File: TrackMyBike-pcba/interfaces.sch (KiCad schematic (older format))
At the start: 1 part

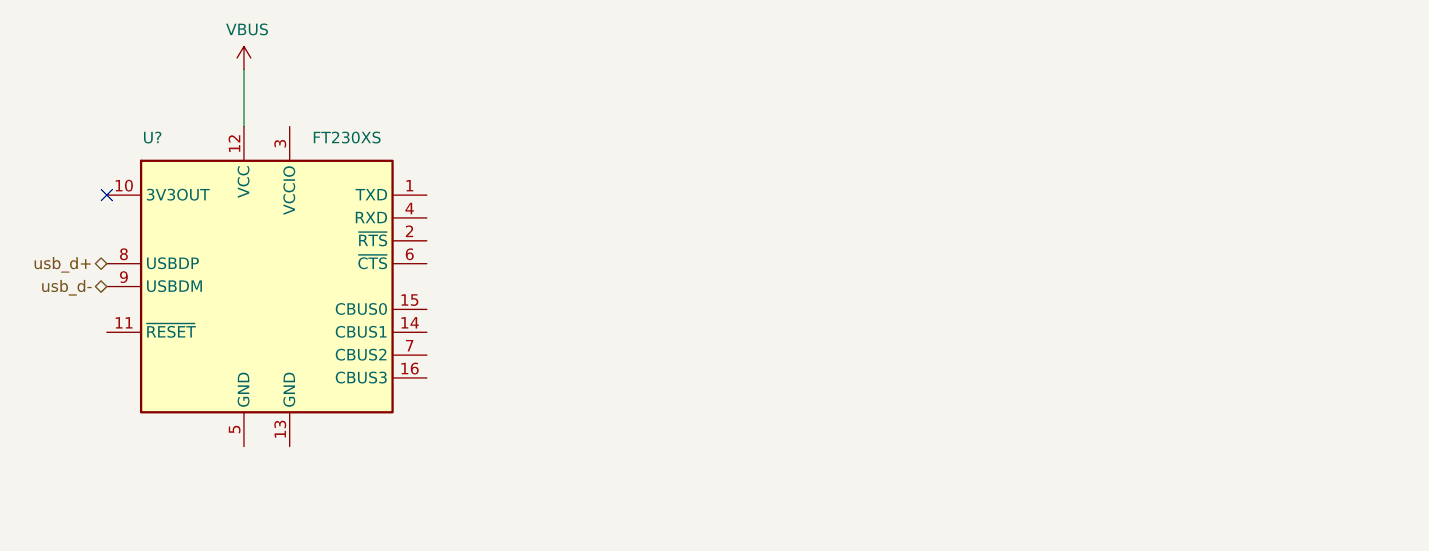
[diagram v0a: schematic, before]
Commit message: Add SIM card, FTDI IC
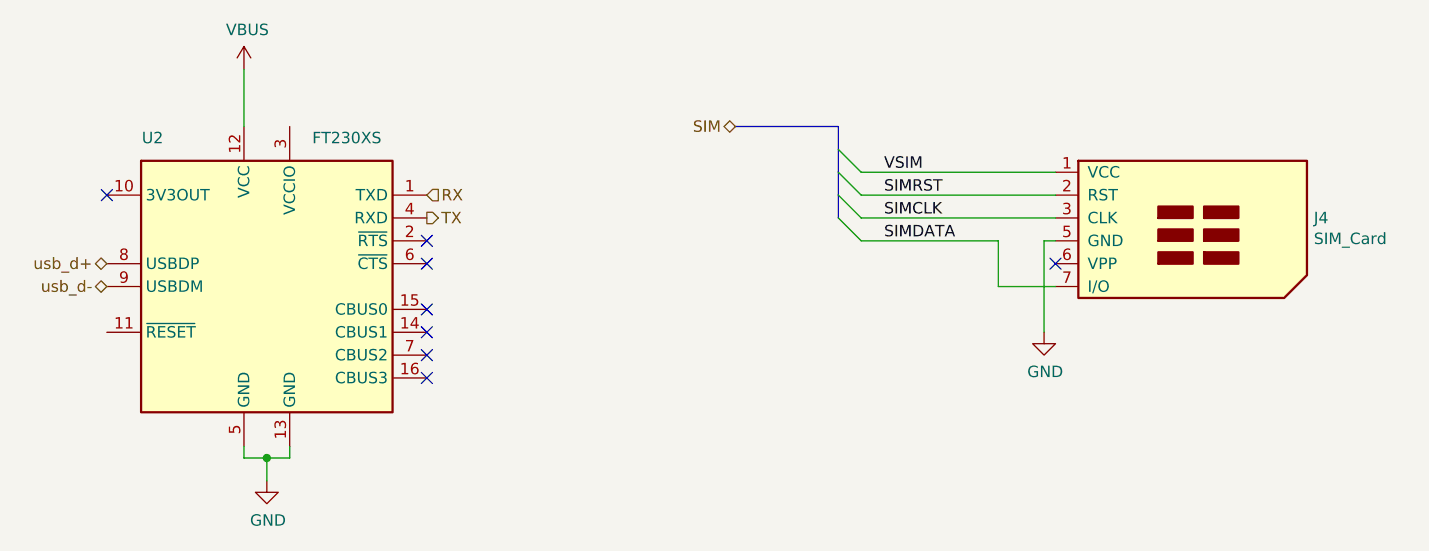
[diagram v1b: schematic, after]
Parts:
- added J4: SIM_Card, symbol Connector:SIM_Card
- gave numbers to parts that had none: 1
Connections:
- net RX: now reaches U2.1 (TXD)
- net GND: now reaches U2.13 (GND)
- net GND: now also U2.5 (GND), J4.5 (GND)
- net TX: now reaches U2.4 (RXD)
- new net SIMCLK: J4.3 (CLK)
- new net SIMDATA: J4.7 (I/O)
- new net SIMRST: J4.2 (RST)
- new net VSIM: J4.1 (VCC)
- no-connect marks 1 -> 8
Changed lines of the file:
@@
 P 3150 2100
 AR Path="/5F19CCC0" Ref="U?"  Part="1"
-AR Path="/5F19B71B/5F19CCC0" Ref="U?"  Part="1"
-F 0 "U?" H 2650 2750 50  0000 C CNN
+AR Path="/5F19B71B/5F19CCC0" Ref="U2"  Part="1"
+F 0 "U2" H 2650 2750 50  0000 C CNN
 F 1 "FT230XS" H 3500 2750 50  0000 C CNN
 F 2 "Package_SO:SSOP-16_3.9x4.9mm_P0.635mm" H 4150 1500 50  0001 C CNN
@@
 P 3050 1150
 AR Path="/5F19CCBA" Ref="#PWR?"  Part="1"
-AR Path="/5F19B71B/5F19CCBA" Ref="#PWR?"  Part="1"
-F 0 "#PWR?" H 3050 1000 50  0001 C CNN
+AR Path="/5F19B71B/5F19CCBA" Ref="#PWR0108"  Part="1"
+F 0 "#PWR0108" H 3050 1000 50  0001 C CNN
 F 1 "VBUS" H 3065 1323 50  0000 C CNN
 F 2 "" H 3050 1150 50  0001 C CNN
@@
 Text HLabel 2450 2100 0    50   BiDi ~ 0
 usb_d-
+Text HLabel 3850 1700 2    50   Input ~ 0
+RX
+Text HLabel 3850 1800 2    50   Output ~ 0
+TX
+$Comp
+L Connector:SIM_Card J4
+U 1 1 5F183DE1
+P 7100 1900
+F 0 "J4" H 7730 2000 50  0000 L CNN
+F 1 "SIM_Card" H 7730 1909 50  0000 L CNN
+F 2 "" H 7100 2250 50  0001 C CNN
+F 3 " ~" H 7050 1900 50  0001 C CNN
+	1    7100 1900
+	1    0    0    -1
+$EndComp
+Text Label 5850 1600 0    50   ~ 0
+VSIM
+Text Label 5850 1700 0    50   ~ 0
+SIMRST
+Text Label 5850 1800 0    50   ~ 0
+SIMCLK
+Text Label 5850 1900 0    50   ~ 0
+SIMDATA
+NoConn ~ 6600 2000
+$Comp
+L power:GND #PWR0109
+U 1 1 5F184986
+P 6550 2300
+F 0 "#PWR0109" H 6550 2050 50  0001 C CNN
+F 1 "GND" H 6555 2127 50  0000 C CNN
+F 2 "" H 6550 2300 50  0001 C CNN
+F 3 "" H 6550 2300 50  0001 C CNN
+	1    6550 2300
+	1    0    0    -1
+$EndComp
+Wire Wire Line
+	6550 2300 6550 1900
+Wire Wire Line
+	6550 1900 6600 1900
+Text HLabel 5200 1400 0    50   BiDi ~ 0
+SIM
+Wire Bus Line
+	5200 1400 5650 1400
+Wire Wire Line
+	5750 1600 6600 1600
+Wire Wire Line
+	5750 1700 6600 1700
+Wire Wire Line
+	5750 1800 6600 1800
+Entry Wire Line
+	5650 1500 5750 1600
+Entry Wire Line
+	5650 1600 5750 1700
+Entry Wire Line
+	5650 1700 5750 1800
+Entry Wire Line
+	5650 1800 5750 1900
+Wire Wire Line
+	6350 1900 6350 2100
+Wire Wire Line
+	6350 2100 6600 2100
+Wire Wire Line
+	5750 1900 6350 1900
+NoConn ~ 3850 1900
+NoConn ~ 3850 2000
+$Comp
+L power:GND #PWR0110
+U 1 1 5F192E7A
+P 3150 2950
+F 0 "#PWR0110" H 3150 2700 50  0001 C CNN
+F 1 "GND" H 3155 2777 50  0000 C CNN
+F 2 "" H 3150 2950 50  0001 C CNN
+F 3 "" H 3150 2950 50  0001 C CNN
+	1    3150 2950
+	1    0    0    -1
+$EndComp
+Wire Wire Line
+	3150 2950 3150 2850
+Wire Wire Line
+	3150 2850 3050 2850
+Wire Wire Line
+	3050 2850 3050 2800
+Wire Wire Line
+	3150 2850 3250 2850
+Wire Wire Line
+	3250 2850 3250 2800
+Connection ~ 3150 2850
+NoConn ~ 3850 2200
+NoConn ~ 3850 2300
+NoConn ~ 3850 2400
+NoConn ~ 3850 2500
+Wire Bus Line
+	5650 1400 5650 1800
 $EndSCHEMATC
